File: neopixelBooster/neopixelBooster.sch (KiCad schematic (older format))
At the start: 12 parts, among them U1 TPS54331

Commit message: Finish schematic, maybe finish routing
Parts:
- removed C5: 10u, Capacitor_SMD:C_0603_1608Metric, symbol Device:C
- removed C6: 47u, Capacitor_SMD:C_0603_1608Metric, symbol Device:C
- removed D1: B340, Diode_SMD:D_SMC, symbol Diode:B340
- removed R4: 10k, Resistor_SMD:R_0603_1608Metric, symbol Device:R
- removed R5: 1k8, Resistor_SMD:R_0603_1608Metric, symbol Device:R
- removed U1: TPS54331, Package_SO:SOIC-8_3.9x4.9mm_P1.27mm, symbol symbols:TPS54331
- added J1, J2: +12, neopixelBooster:InputPads, symbol Connector_Generic:Conn_01x01
- added J3, J4: GND, neopixelBooster:InputPads, symbol Connector_Generic:Conn_01x01
- added J5: ESP_INPUT, neopixelBooster:3PinConnector, symbol Connector_Generic:Conn_01x03
- added P1, P2: NeopixelStripPads, neopixelBooster:LedStripPads, symbol symbols:NeopixelStripPads
- added R1: 200k, Resistor_SMD:R_0402_1005Metric, symbol Device:R
- added R3: 27k, Resistor_SMD:R_0402_1005Metric, symbol Device:R
- added U1: SY8105, Package_TO_SOT_SMD:TSOT-23-6, symbol symbols:SY8105
- C1: value 10n -> 10u; footprint Capacitor_SMD:C_0603_1608Metric -> Capacitor_SMD:C_0805_2012Metric
- C2: value 10p -> 100n; footprint Capacitor_SMD:C_0603_1608Metric -> Capacitor_SMD:C_0402_1005Metric
- C3: value 2n2 -> 47p; footprint Capacitor_SMD:C_0603_1608Metric -> Capacitor_SMD:C_0402_1005Metric
- C4: value 100n -> 22u
- L1: value 10u -> 4u7; footprint (none) -> neopixelBooster:SMNR8040
- R2: value 15k -> 27k; footprint Resistor_SMD:R_0603_1608Metric -> Resistor_SMD:R_0402_1005Metric
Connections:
- net labels added: DATA
- wire segments 43 -> 50
- no-connect marks 0 -> 1

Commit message: Finish routing v1.0
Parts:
- added D1: LED, LED_SMD:LED_0603_1608Metric, symbol Device:LED
- added R4: 47k, Resistor_SMD:R_0402_1005Metric, symbol Device:R
- C1: MFR (none) -> CL21A106KAYNNNE
- C2: MFR (none) -> CL05B104KO5NNNC
- C3: MFR (none) -> 0402CG470J500NT
- C4: MFR (none) -> CL10A226MQ8NRNC
- L1: footprint neopixelBooster:SMNR8040 -> neopixelBooster:MWSA0503S; MFR (none) -> MWSA0503S-4R7MT
- R1: MFR (none) -> 0402WGF2003TCE
- R2, R3: MFR (none) -> 0402WGF2702TCE
- U1: MFR (none) -> SY8105ADC
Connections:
- net +5V: now also R4.1
- net GND: now also D1.1 (K)
- new net: D1.2 (A), R4.2
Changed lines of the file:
@@
 F 2 "Package_TO_SOT_SMD:TSOT-23-6" H 4000 2250 50  0001 C CNN
 F 3 "" H 3300 2600 50  0001 C CNN
+F 4 "SY8105ADC" H 3300 2600 50  0001 C CNN "MFR"
 	1    3300 2600
 	1    0    0    -1
@@
 F 2 "Resistor_SMD:R_0402_1005Metric" V 4030 2550 50  0001 C CNN
 F 3 "~" H 4100 2550 50  0001 C CNN
+F 4 "0402WGF2003TCE" H 4100 2550 50  0001 C CNN "MFR"
 	1    4100 2550
 	1    0    0    -1
@@
 F 2 "Resistor_SMD:R_0402_1005Metric" V 4030 3050 50  0001 C CNN
 F 3 "~" H 4100 3050 50  0001 C CNN
+F 4 "0402WGF2702TCE" H 4100 3050 50  0001 C CNN "MFR"
 	1    4100 3050
 	1    0    0    -1
@@
 F 2 "Capacitor_SMD:C_0805_2012Metric" H 2538 2400 50  0001 C CNN
 F 3 "~" H 2500 2550 50  0001 C CNN
+F 4 "CL21A106KAYNNNE" H 2500 2550 50  0001 C CNN "MFR"
 	1    2500 2550
 	1    0    0    -1
@@
 F 2 "Capacitor_SMD:C_0402_1005Metric" H 3538 1900 50  0001 C CNN
 F 3 "~" H 3500 2050 50  0001 C CNN
+F 4 "CL05B104KO5NNNC" H 3500 2050 50  0001 C CNN "MFR"
 	1    3500 2050
 	0    1    1    0
@@
 F 0 "L1" V 4090 2300 50  0000 C CNN
 F 1 "4u7" V 3999 2300 50  0000 C CNN
-F 2 "neopixelBooster:SMNR8040" H 3900 2300 50  0001 C CNN
+F 2 "neopixelBooster:MWSA0503S" H 3900 2300 50  0001 C CNN
 F 3 "~" H 3900 2300 50  0001 C CNN
+F 4 "MWSA0503S-4R7MT" H 3900 2300 50  0001 C CNN "MFR"
 	1    3900 2300
 	0    -1   -1   0
@@
 F 2 "Capacitor_SMD:C_0402_1005Metric" H 4538 2400 50  0001 C CNN
 F 3 "~" H 4500 2550 50  0001 C CNN
+F 4 "0402CG470J500NT" H 4500 2550 50  0001 C CNN "MFR"
 	1    4500 2550
 	-1   0    0    1
@@
 F 2 "Capacitor_SMD:C_0603_1608Metric" H 4988 2400 50  0001 C CNN
 F 3 "~" H 4950 2550 50  0001 C CNN
+F 4 "CL10A226MQ8NRNC" H 4950 2550 50  0001 C CNN "MFR"
 	1    4950 2550
 	-1   0    0    1
@@
 F 2 "Resistor_SMD:R_0402_1005Metric" V 2780 2550 50  0001 C CNN
 F 3 "~" H 2850 2550 50  0001 C CNN
+F 4 "0402WGF2702TCE" H 2850 2550 50  0001 C CNN "MFR"
 	1    2850 2550
 	1    0    0    -1
@@
 Wire Wire Line
 	3150 1450 3550 1450
+$Comp
+L Device:LED D1
+U 1 1 5F11ED7A
+P 6550 2250
+F 0 "D1" V 6589 2133 50  0000 R CNN
+F 1 "LED" V 6498 2133 50  0000 R CNN
+F 2 "LED_SMD:LED_0603_1608Metric" H 6550 2250 50  0001 C CNN
+F 3 "~" H 6550 2250 50  0001 C CNN
+F 4 "KT-0603R" H 6550 2250 50  0001 C CNN "MFR"
+	1    6550 2250
+	0    -1   -1   0
+$EndComp
+$Comp
+L power:+5V #PWR06
+U 1 1 5F120EBB
+P 6550 1700
+F 0 "#PWR06" H 6550 1550 50  0001 C CNN
+F 1 "+5V" H 6565 1873 50  0000 C CNN
+F 2 "" H 6550 1700 50  0001 C CNN
+F 3 "" H 6550 1700 50  0001 C CNN
+	1    6550 1700
+	1    0    0    -1
+$EndComp
+$Comp
+L power:GND #PWR07
+U 1 1 5F12144C
+P 6550 2500
+F 0 "#PWR07" H 6550 2250 50  0001 C CNN
+F 1 "GND" H 6555 2327 50  0000 C CNN
+F 2 "" H 6550 2500 50  0001 C CNN
+F 3 "" H 6550 2500 50  0001 C CNN
+	1    6550 2500
+	1    0    0    -1
+$EndComp
+Wire Wire Line
+	6550 2050 6550 2100
+Wire Wire Line
+	6550 1700 6550 1750
+Wire Wire Line
+	6550 2400 6550 2500
+$Comp
+L Device:R R4
+U 1 1 5F120876
+P 6550 1900
+F 0 "R4" H 6620 1946 50  0000 L CNN
+F 1 "47k" H 6620 1855 50  0000 L CNN
+F 2 "Resistor_SMD:R_0402_1005Metric" V 6480 1900 50  0001 C CNN
+F 3 "~" H 6550 1900 50  0001 C CNN
+F 4 "0402WGF4702TCE" H 6550 1900 50  0001 C CNN "MFR"
+	1    6550 1900
+	1    0    0    -1
+$EndComp
 $EndSCHEMATC

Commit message: Rename MFR field to LSCS
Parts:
- C1: LCSC (none) -> CL21A106KAYNNNE; MFR CL21A106KAYNNNE -> (none)
- C2: LCSC (none) -> CL05B104KO5NNNC; MFR CL05B104KO5NNNC -> (none)
- C3: LCSC (none) -> 0402CG470J500NT; MFR 0402CG470J500NT -> (none)
- C4: LCSC (none) -> CL10A226MQ8NRNC; MFR CL10A226MQ8NRNC -> (none)
- D1: LCSC (none) -> KT-0603R; MFR KT-0603R -> (none)
- L1: LCSC (none) -> MWSA0503S-4R7MT; MFR MWSA0503S-4R7MT -> (none)
- R1: LCSC (none) -> 0402WGF2003TCE; MFR 0402WGF2003TCE -> (none)
- R2, R3: LCSC (none) -> 0402WGF2702TCE; MFR 0402WGF2702TCE -> (none)
- R4: LCSC (none) -> 0402WGF4702TCE; MFR 0402WGF4702TCE -> (none)
- U1: LCSC (none) -> SY8105ADC; MFR SY8105ADC -> (none)
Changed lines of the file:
@@
 F 2 "Package_TO_SOT_SMD:TSOT-23-6" H 4000 2250 50  0001 C CNN
 F 3 "" H 3300 2600 50  0001 C CNN
-F 4 "SY8105ADC" H 3300 2600 50  0001 C CNN "MFR"
+F 4 "SY8105ADC" H 3300 2600 50  0001 C CNN "LCSC"
 	1    3300 2600
 	1    0    0    -1
@@
 F 2 "Resistor_SMD:R_0402_1005Metric" V 4030 2550 50  0001 C CNN
 F 3 "~" H 4100 2550 50  0001 C CNN
-F 4 "0402WGF2003TCE" H 4100 2550 50  0001 C CNN "MFR"
+F 4 "0402WGF2003TCE" H 4100 2550 50  0001 C CNN "LCSC"
 	1    4100 2550
 	1    0    0    -1
@@
 F 2 "Resistor_SMD:R_0402_1005Metric" V 4030 3050 50  0001 C CNN
 F 3 "~" H 4100 3050 50  0001 C CNN
-F 4 "0402WGF2702TCE" H 4100 3050 50  0001 C CNN "MFR"
+F 4 "0402WGF2702TCE" H 4100 3050 50  0001 C CNN "LCSC"
 	1    4100 3050
 	1    0    0    -1
@@
 F 2 "Capacitor_SMD:C_0805_2012Metric" H 2538 2400 50  0001 C CNN
 F 3 "~" H 2500 2550 50  0001 C CNN
-F 4 "CL21A106KAYNNNE" H 2500 2550 50  0001 C CNN "MFR"
+F 4 "CL21A106KAYNNNE" H 2500 2550 50  0001 C CNN "LCSC"
 	1    2500 2550
 	1    0    0    -1
@@
 F 2 "Capacitor_SMD:C_0402_1005Metric" H 3538 1900 50  0001 C CNN
 F 3 "~" H 3500 2050 50  0001 C CNN
-F 4 "CL05B104KO5NNNC" H 3500 2050 50  0001 C CNN "MFR"
+F 4 "CL05B104KO5NNNC" H 3500 2050 50  0001 C CNN "LCSC"
 	1    3500 2050
 	0    1    1    0
@@
 F 2 "neopixelBooster:MWSA0503S" H 3900 2300 50  0001 C CNN
 F 3 "~" H 3900 2300 50  0001 C CNN
-F 4 "MWSA0503S-4R7MT" H 3900 2300 50  0001 C CNN "MFR"
+F 4 "MWSA0503S-4R7MT" H 3900 2300 50  0001 C CNN "LCSC"
 	1    3900 2300
 	0    -1   -1   0
@@
 F 2 "Capacitor_SMD:C_0402_1005Metric" H 4538 2400 50  0001 C CNN
 F 3 "~" H 4500 2550 50  0001 C CNN
-F 4 "0402CG470J500NT" H 4500 2550 50  0001 C CNN "MFR"
+F 4 "0402CG470J500NT" H 4500 2550 50  0001 C CNN "LCSC"
 	1    4500 2550
 	-1   0    0    1
@@
 F 2 "Capacitor_SMD:C_0603_1608Metric" H 4988 2400 50  0001 C CNN
 F 3 "~" H 4950 2550 50  0001 C CNN
-F 4 "CL10A226MQ8NRNC" H 4950 2550 50  0001 C CNN "MFR"
+F 4 "CL10A226MQ8NRNC" H 4950 2550 50  0001 C CNN "LCSC"
 	1    4950 2550
 	-1   0    0    1
@@
 F 2 "Resistor_SMD:R_0402_1005Metric" V 2780 2550 50  0001 C CNN
 F 3 "~" H 2850 2550 50  0001 C CNN
-F 4 "0402WGF2702TCE" H 2850 2550 50  0001 C CNN "MFR"
+F 4 "0402WGF2702TCE" H 2850 2550 50  0001 C CNN "LCSC"
 	1    2850 2550
 	1    0    0    -1
@@
 F 2 "LED_SMD:LED_0603_1608Metric" H 6550 2250 50  0001 C CNN
 F 3 "~" H 6550 2250 50  0001 C CNN
-F 4 "KT-0603R" H 6550 2250 50  0001 C CNN "MFR"
+F 4 "KT-0603R" H 6550 2250 50  0001 C CNN "LCSC"
 	1    6550 2250
 	0    -1   -1   0
@@
 F 2 "Resistor_SMD:R_0402_1005Metric" V 6480 1900 50  0001 C CNN
 F 3 "~" H 6550 1900 50  0001 C CNN
-F 4 "0402WGF4702TCE" H 6550 1900 50  0001 C CNN "MFR"
+F 4 "0402WGF4702TCE" H 6550 1900 50  0001 C CNN "LCSC"
 	1    6550 1900
 	1    0    0    -1

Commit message: Use LSCS numbers
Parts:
- C1: LCSC CL21A106KAYNNNE -> C1525
- C2: LCSC CL05B104KO5NNNC -> C1525
- C3: LCSC 0402CG470J500NT -> C1567
- C4: LCSC CL10A226MQ8NRNC -> C59461
- D1: LCSC KT-0603R -> C2286
- L1: LCSC MWSA0503S-4R7MT -> C408410
- R1: LCSC 0402WGF2003TCE -> C25764
- R2, R3: LCSC 0402WGF2702TCE -> C25771
- R4: LCSC 0402WGF4702TCE -> C25792
- U1: LCSC SY8105ADC -> C178247
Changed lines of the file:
@@
 EESchema Schematic File Version 4
-LIBS:neopixelBooster-cache
-EELAYER 29 0
+EELAYER 30 0
 EELAYER END
 $Descr A4 11693 8268
@@
 F 2 "Package_TO_SOT_SMD:TSOT-23-6" H 4000 2250 50  0001 C CNN
 F 3 "" H 3300 2600 50  0001 C CNN
-F 4 "SY8105ADC" H 3300 2600 50  0001 C CNN "LCSC"
+F 4 "C178247 " H 3300 2600 50  0001 C CNN "LCSC"
 	1    3300 2600
 	1    0    0    -1
@@
 F 2 "Resistor_SMD:R_0402_1005Metric" V 4030 2550 50  0001 C CNN
 F 3 "~" H 4100 2550 50  0001 C CNN
-F 4 "0402WGF2003TCE" H 4100 2550 50  0001 C CNN "LCSC"
+F 4 "C25764" H 4100 2550 50  0001 C CNN "LCSC"
 	1    4100 2550
 	1    0    0    -1
@@
 F 2 "Resistor_SMD:R_0402_1005Metric" V 4030 3050 50  0001 C CNN
 F 3 "~" H 4100 3050 50  0001 C CNN
-F 4 "0402WGF2702TCE" H 4100 3050 50  0001 C CNN "LCSC"
+F 4 "C25771" H 4100 3050 50  0001 C CNN "LCSC"
 	1    4100 3050
 	1    0    0    -1
@@
 F 2 "Capacitor_SMD:C_0805_2012Metric" H 2538 2400 50  0001 C CNN
 F 3 "~" H 2500 2550 50  0001 C CNN
-F 4 "CL21A106KAYNNNE" H 2500 2550 50  0001 C CNN "LCSC"
+F 4 "C1525" H 2500 2550 50  0001 C CNN "LCSC"
 	1    2500 2550
 	1    0    0    -1
@@
 F 2 "Capacitor_SMD:C_0402_1005Metric" H 3538 1900 50  0001 C CNN
 F 3 "~" H 3500 2050 50  0001 C CNN
-F 4 "CL05B104KO5NNNC" H 3500 2050 50  0001 C CNN "LCSC"
+F 4 "C1525" H 3500 2050 50  0001 C CNN "LCSC"
 	1    3500 2050
 	0    1    1    0
@@
 F 2 "neopixelBooster:MWSA0503S" H 3900 2300 50  0001 C CNN
 F 3 "~" H 3900 2300 50  0001 C CNN
-F 4 "MWSA0503S-4R7MT" H 3900 2300 50  0001 C CNN "LCSC"
+F 4 "C408410" H 3900 2300 50  0001 C CNN "LCSC"
 	1    3900 2300
 	0    -1   -1   0
@@
 F 2 "Capacitor_SMD:C_0402_1005Metric" H 4538 2400 50  0001 C CNN
 F 3 "~" H 4500 2550 50  0001 C CNN
-F 4 "0402CG470J500NT" H 4500 2550 50  0001 C CNN "LCSC"
+F 4 "C1567" H 4500 2550 50  0001 C CNN "LCSC"
 	1    4500 2550
 	-1   0    0    1
@@
 F 2 "Capacitor_SMD:C_0603_1608Metric" H 4988 2400 50  0001 C CNN
 F 3 "~" H 4950 2550 50  0001 C CNN
-F 4 "CL10A226MQ8NRNC" H 4950 2550 50  0001 C CNN "LCSC"
+F 4 "C59461" H 4950 2550 50  0001 C CNN "LCSC"
 	1    4950 2550
 	-1   0    0    1
@@
 F 2 "Resistor_SMD:R_0402_1005Metric" V 2780 2550 50  0001 C CNN
 F 3 "~" H 2850 2550 50  0001 C CNN
-F 4 "0402WGF2702TCE" H 2850 2550 50  0001 C CNN "LCSC"
+F 4 "C25771" H 2850 2550 50  0001 C CNN "LCSC"
 	1    2850 2550
 	1    0    0    -1
@@
 F 2 "LED_SMD:LED_0603_1608Metric" H 6550 2250 50  0001 C CNN
 F 3 "~" H 6550 2250 50  0001 C CNN
-F 4 "KT-0603R" H 6550 2250 50  0001 C CNN "LCSC"
+F 4 "C2286" H 6550 2250 50  0001 C CNN "LCSC"
 	1    6550 2250
 	0    -1   -1   0
@@
 F 2 "Resistor_SMD:R_0402_1005Metric" V 6480 1900 50  0001 C CNN
 F 3 "~" H 6550 1900 50  0001 C CNN
-F 4 "0402WGF4702TCE" H 6550 1900 50  0001 C CNN "LCSC"
+F 4 "C25792" H 6550 1900 50  0001 C CNN "LCSC"
 	1    6550 1900
 	1    0    0    -1

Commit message: Fix assembly data
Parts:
- C1: LCSC C1525 -> C1046
- U1: JLCPCB_CORRECTION (none) -> 0;0;180
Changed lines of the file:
@@
 F 3 "" H 3300 2600 50  0001 C CNN
 F 4 "C178247 " H 3300 2600 50  0001 C CNN "LCSC"
+F 5 "0;0;180" H 3300 2600 50  0001 C CNN "JLCPCB_CORRECTION"
 	1    3300 2600
 	1    0    0    -1
@@
 F 2 "Capacitor_SMD:C_0805_2012Metric" H 2538 2400 50  0001 C CNN
 F 3 "~" H 2500 2550 50  0001 C CNN
-F 4 "C1525" H 2500 2550 50  0001 C CNN "LCSC"
+F 4 "C1046" H 2500 2550 50  0001 C CNN "LCSC"
 	1    2500 2550
 	1    0    0    -1

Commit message: Fixed errors of version 1.0
- C1 changed LCSC code
- C2 changed to 0603 100nF/50V
- C4 changed to 0805 22uF/25V
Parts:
- C1: LCSC C1046 -> C15850
- C2: footprint Capacitor_SMD:C_0402_1005Metric -> Capacitor_SMD:C_0603_1608Metric; LCSC C1525 -> C14663
- C4: footprint Capacitor_SMD:C_0603_1608Metric -> Capacitor_SMD:C_0805_2012Metric; LCSC C59461 -> C45783
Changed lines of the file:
@@
 F 2 "Capacitor_SMD:C_0805_2012Metric" H 2538 2400 50  0001 C CNN
 F 3 "~" H 2500 2550 50  0001 C CNN
-F 4 "C1046" H 2500 2550 50  0001 C CNN "LCSC"
+F 4 "C15850" H 2500 2550 50  0001 C CNN "LCSC"
 	1    2500 2550
 	1    0    0    -1
@@
 F 0 "C2" V 3248 2050 50  0000 C CNN
 F 1 "100n" V 3339 2050 50  0000 C CNN
-F 2 "Capacitor_SMD:C_0402_1005Metric" H 3538 1900 50  0001 C CNN
+F 2 "Capacitor_SMD:C_0603_1608Metric" H 3538 1900 50  0001 C CNN
 F 3 "~" H 3500 2050 50  0001 C CNN
-F 4 "C1525" H 3500 2050 50  0001 C CNN "LCSC"
+F 4 "C14663" H 3500 2050 50  0001 C CNN "LCSC"
 	1    3500 2050
 	0    1    1    0
@@
 F 0 "C4" H 4835 2504 50  0000 R CNN
 F 1 "22u" H 4835 2595 50  0000 R CNN
-F 2 "Capacitor_SMD:C_0603_1608Metric" H 4988 2400 50  0001 C CNN
+F 2 "Capacitor_SMD:C_0805_2012Metric" H 4988 2400 50  0001 C CNN
 F 3 "~" H 4950 2550 50  0001 C CNN
-F 4 "C59461" H 4950 2550 50  0001 C CNN "LCSC"
+F 4 "C45783" H 4950 2550 50  0001 C CNN "LCSC"
 	1    4950 2550
 	-1   0    0    1

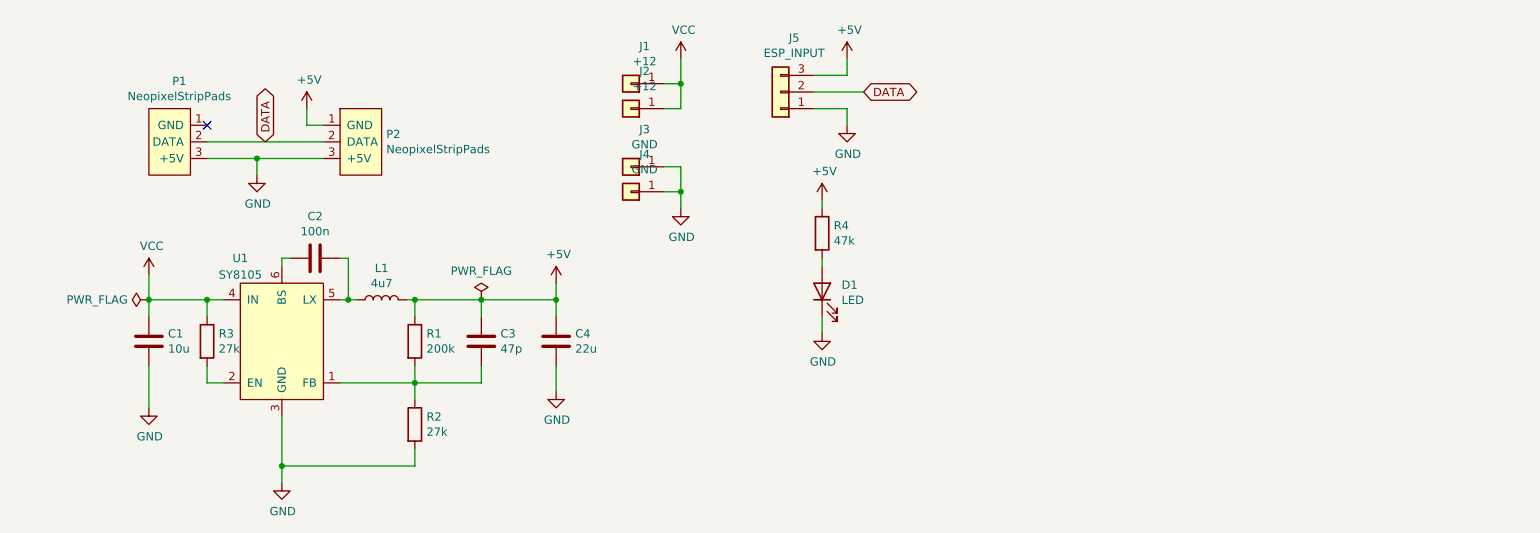
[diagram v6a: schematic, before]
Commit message: Initial layout of v2.0
- Increased size of board to 26 x 10 mm
- Swap pins for connecting Neopixel strip
- Add filtration to input and output
- Change shape of input pads
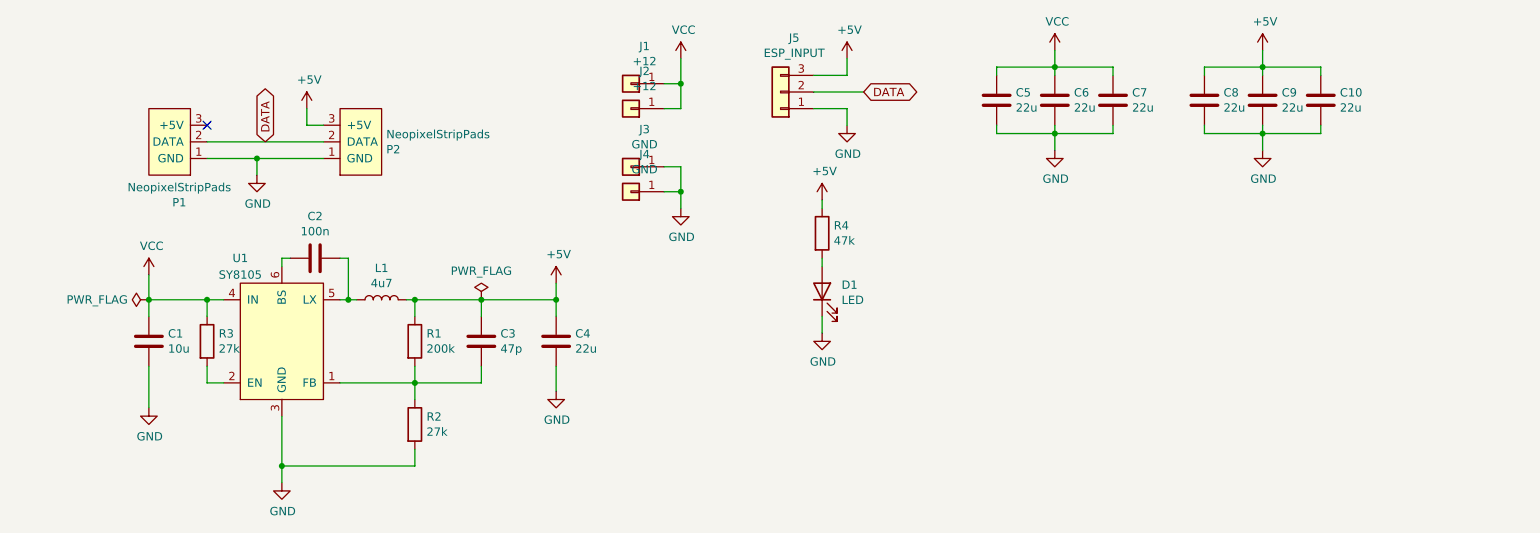
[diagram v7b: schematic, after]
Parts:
- added C10, C5, C6, C7, C8, C9: 22u, Capacitor_SMD:C_0805_2012Metric, symbol Device:C
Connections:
- net +5V: now also P2.3 (+5V), C10.1, C8.1, C9.1; no longer P2.1 (GND)
- net GND: now also P1.1 (GND), P2.1 (GND), C10.2, C5.2, C6.2, C7.2, C8.2, C9.2; no longer P1.3 (+5V), P2.3 (+5V)
- net VCC: now also C5.1, C6.1, C7.1
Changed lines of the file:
@@
 L symbols:NeopixelStripPads P1
 U 1 1 5F1483D2
-P 2750 1600
-F 0 "P1" H 2817 2215 50  0000 C CNN
-F 1 "NeopixelStripPads" H 2817 2124 50  0000 C CNN
-F 2 "neopixelBooster:LedStripPads" H 2750 1600 50  0001 C CNN
-F 3 "" H 2750 1600 50  0001 C CNN
-	1    2750 1600
-	-1   0    0    -1
+P 2750 1100
+F 0 "P1" H 2817 1715 50  0000 C CNN
+F 1 "NeopixelStripPads" H 2817 1624 50  0000 C CNN
+F 2 "neopixelBooster:LedStripPads" H 2750 1100 50  0001 C CNN
+F 3 "" H 2750 1100 50  0001 C CNN
+	1    2750 1100
+	-1   0    0    1
 $EndComp
 $Comp
 L symbols:NeopixelStripPads P2
 U 1 1 5F14A4FD
-P 3650 1600
-F 0 "P2" H 3928 1896 50  0000 L CNN
-F 1 "NeopixelStripPads" H 3928 1805 50  0000 L CNN
-F 2 "neopixelBooster:LedStripPads" H 3650 1600 50  0001 C CNN
-F 3 "" H 3650 1600 50  0001 C CNN
-	1    3650 1600
-	1    0    0    -1
+P 3650 1100
+F 0 "P2" H 3928 1396 50  0000 L CNN
+F 1 "NeopixelStripPads" H 3928 1305 50  0000 L CNN
+F 2 "neopixelBooster:LedStripPads" H 3650 1100 50  0001 C CNN
+F 3 "" H 3650 1100 50  0001 C CNN
+	1    3650 1100
+	1    0    0    1
 $EndComp
 Wire Wire Line
@@
 	1    0    0    -1
 $EndComp
+$Comp
+L power:VCC #PWR08
+U 1 1 5FB1CA2C
+P 7950 800
+F 0 "#PWR08" H 7950 650 50  0001 C CNN
+F 1 "VCC" H 7965 973 50  0000 C CNN
+F 2 "" H 7950 800 50  0001 C CNN
+F 3 "" H 7950 800 50  0001 C CNN
+	1    7950 800
+	1    0    0    -1
+$EndComp
+$Comp
+L power:GND #PWR09
+U 1 1 5FB1EBDF
+P 7950 1400
+F 0 "#PWR09" H 7950 1150 50  0001 C CNN
+F 1 "GND" H 7955 1227 50  0000 C CNN
+F 2 "" H 7950 1400 50  0001 C CNN
+F 3 "" H 7950 1400 50  0001 C CNN
+	1    7950 1400
+	1    0    0    -1
+$EndComp
+$Comp
+L power:+5V #PWR010
+U 1 1 5FB1F8F3
+P 9200 800
+F 0 "#PWR010" H 9200 650 50  0001 C CNN
+F 1 "+5V" H 9215 973 50  0000 C CNN
+F 2 "" H 9200 800 50  0001 C CNN
+F 3 "" H 9200 800 50  0001 C CNN
+	1    9200 800
+	1    0    0    -1
+$EndComp
+$Comp
+L power:GND #PWR011
+U 1 1 5FB209DF
+P 9200 1400
+F 0 "#PWR011" H 9200 1150 50  0001 C CNN
+F 1 "GND" H 9205 1227 50  0000 C CNN
+F 2 "" H 9200 1400 50  0001 C CNN
+F 3 "" H 9200 1400 50  0001 C CNN
+	1    9200 1400
+	1    0    0    -1
+$EndComp
+$Comp
+L Device:C C6
+U 1 1 5FB2275D
+P 7950 1100
+F 0 "C6" H 8065 1146 50  0000 L CNN
+F 1 "22u" H 8065 1055 50  0000 L CNN
+F 2 "Capacitor_SMD:C_0805_2012Metric" H 7988 950 50  0001 C CNN
+F 3 "~" H 7950 1100 50  0001 C CNN
+F 4 "C45783" H 7950 1100 50  0001 C CNN "LCSC"
+	1    7950 1100
+	1    0    0    -1
+$EndComp
+$Comp
+L Device:C C7
+U 1 1 5FB230A4
+P 8300 1100
+F 0 "C7" H 8415 1146 50  0000 L CNN
+F 1 "22u" H 8415 1055 50  0000 L CNN
+F 2 "Capacitor_SMD:C_0805_2012Metric" H 8338 950 50  0001 C CNN
+F 3 "~" H 8300 1100 50  0001 C CNN
+F 4 "C45783" H 8300 1100 50  0001 C CNN "LCSC"
+	1    8300 1100
+	1    0    0    -1
+$EndComp
+Wire Wire Line
+	7950 900  7950 800
+Wire Wire Line
+	7950 950  7950 900
+Connection ~ 7950 900
+Wire Wire Line
+	7950 1300 7950 1250
+Connection ~ 7950 1300
+Wire Wire Line
+	7950 1300 7950 1400
+$Comp
+L Device:C C8
+U 1 1 5FB2A640
+P 8850 1100
+F 0 "C8" H 8965 1146 50  0000 L CNN
+F 1 "22u" H 8965 1055 50  0000 L CNN
+F 2 "Capacitor_SMD:C_0805_2012Metric" H 8888 950 50  0001 C CNN
+F 3 "~" H 8850 1100 50  0001 C CNN
+F 4 "C45783" H 8850 1100 50  0001 C CNN "LCSC"
+	1    8850 1100
+	1    0    0    -1
+$EndComp
+$Comp
+L Device:C C9
+U 1 1 5FB2B032
+P 9200 1100
+F 0 "C9" H 9315 1146 50  0000 L CNN
+F 1 "22u" H 9315 1055 50  0000 L CNN
+F 2 "Capacitor_SMD:C_0805_2012Metric" H 9238 950 50  0001 C CNN
+F 3 "~" H 9200 1100 50  0001 C CNN
+F 4 "C45783" H 9200 1100 50  0001 C CNN "LCSC"
+	1    9200 1100
+	1    0    0    -1
+$EndComp
+$Comp
+L Device:C C10
+U 1 1 5FB2B5AE
+P 9550 1100
+F 0 "C10" H 9665 1146 50  0000 L CNN
+F 1 "22u" H 9665 1055 50  0000 L CNN
+F 2 "Capacitor_SMD:C_0805_2012Metric" H 9588 950 50  0001 C CNN
+F 3 "~" H 9550 1100 50  0001 C CNN
+F 4 "C45783" H 9550 1100 50  0001 C CNN "LCSC"
+	1    9550 1100
+	1    0    0    -1
+$EndComp
+Wire Wire Line
+	8850 900  8850 950
+Wire Wire Line
+	9200 900  9200 800
+Wire Wire Line
+	8850 900  9200 900
+Wire Wire Line
+	9200 900  9200 950
+Connection ~ 9200 900
+Wire Wire Line
+	9200 900  9550 900
+Wire Wire Line
+	9550 900  9550 950
+Wire Wire Line
+	8850 1250 8850 1300
+Wire Wire Line
+	8850 1300 9200 1300
+Wire Wire Line
+	9200 1300 9200 1250
+Wire Wire Line
+	9200 1300 9550 1300
+Wire Wire Line
+	9550 1300 9550 1250
+Connection ~ 9200 1300
+Wire Wire Line
+	9200 1300 9200 1400
+Wire Wire Line
+	7600 900  7600 950
+Wire Wire Line
+	7600 900  7950 900
+Wire Wire Line
+	7600 1300 7600 1250
+Wire Wire Line
+	7600 1300 7950 1300
+Wire Wire Line
+	8300 900  8300 950
+Wire Wire Line
+	7950 900  8300 900
+Wire Wire Line
+	8300 1300 8300 1250
+Wire Wire Line
+	7950 1300 8300 1300
+$Comp
+L Device:C C5
+U 1 1 5FB20F2E
+P 7600 1100
+F 0 "C5" H 7715 1146 50  0000 L CNN
+F 1 "22u" H 7715 1055 50  0000 L CNN
+F 2 "Capacitor_SMD:C_0805_2012Metric" H 7638 950 50  0001 C CNN
+F 3 "~" H 7600 1100 50  0001 C CNN
+F 4 "C45783" H 7600 1100 50  0001 C CNN "LCSC"
+	1    7600 1100
+	1    0    0    -1
+$EndComp
